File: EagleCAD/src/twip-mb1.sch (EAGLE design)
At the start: 13 parts, among them U1 GY-521MPU6050

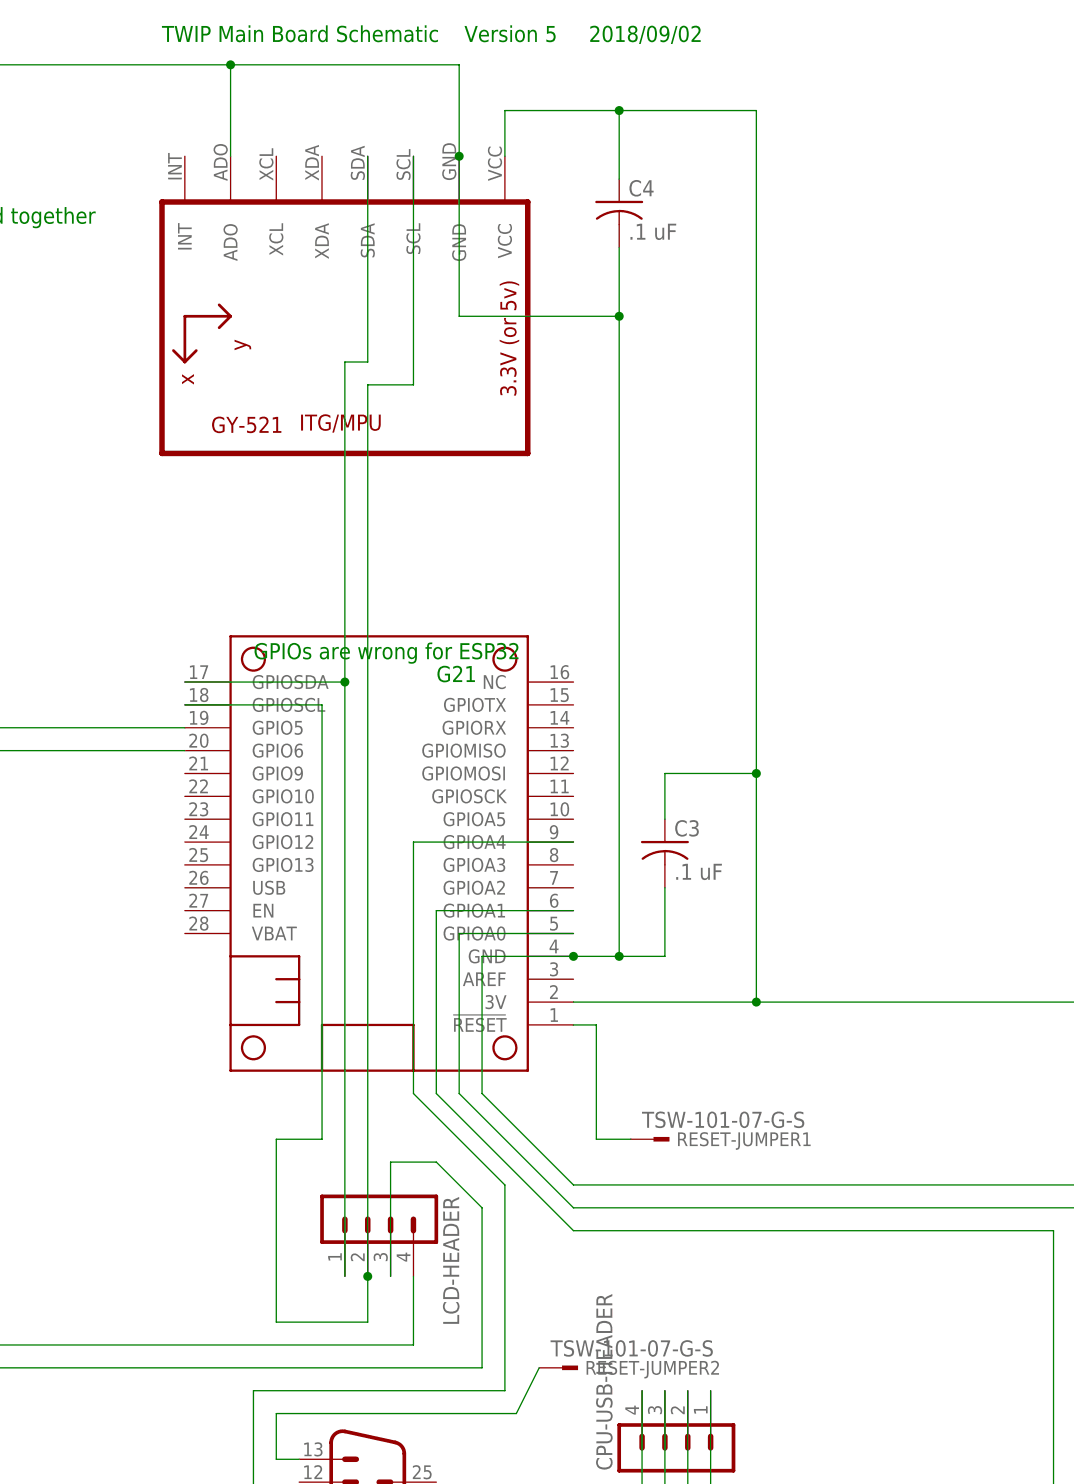
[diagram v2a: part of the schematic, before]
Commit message: separate I2C buses with pullups
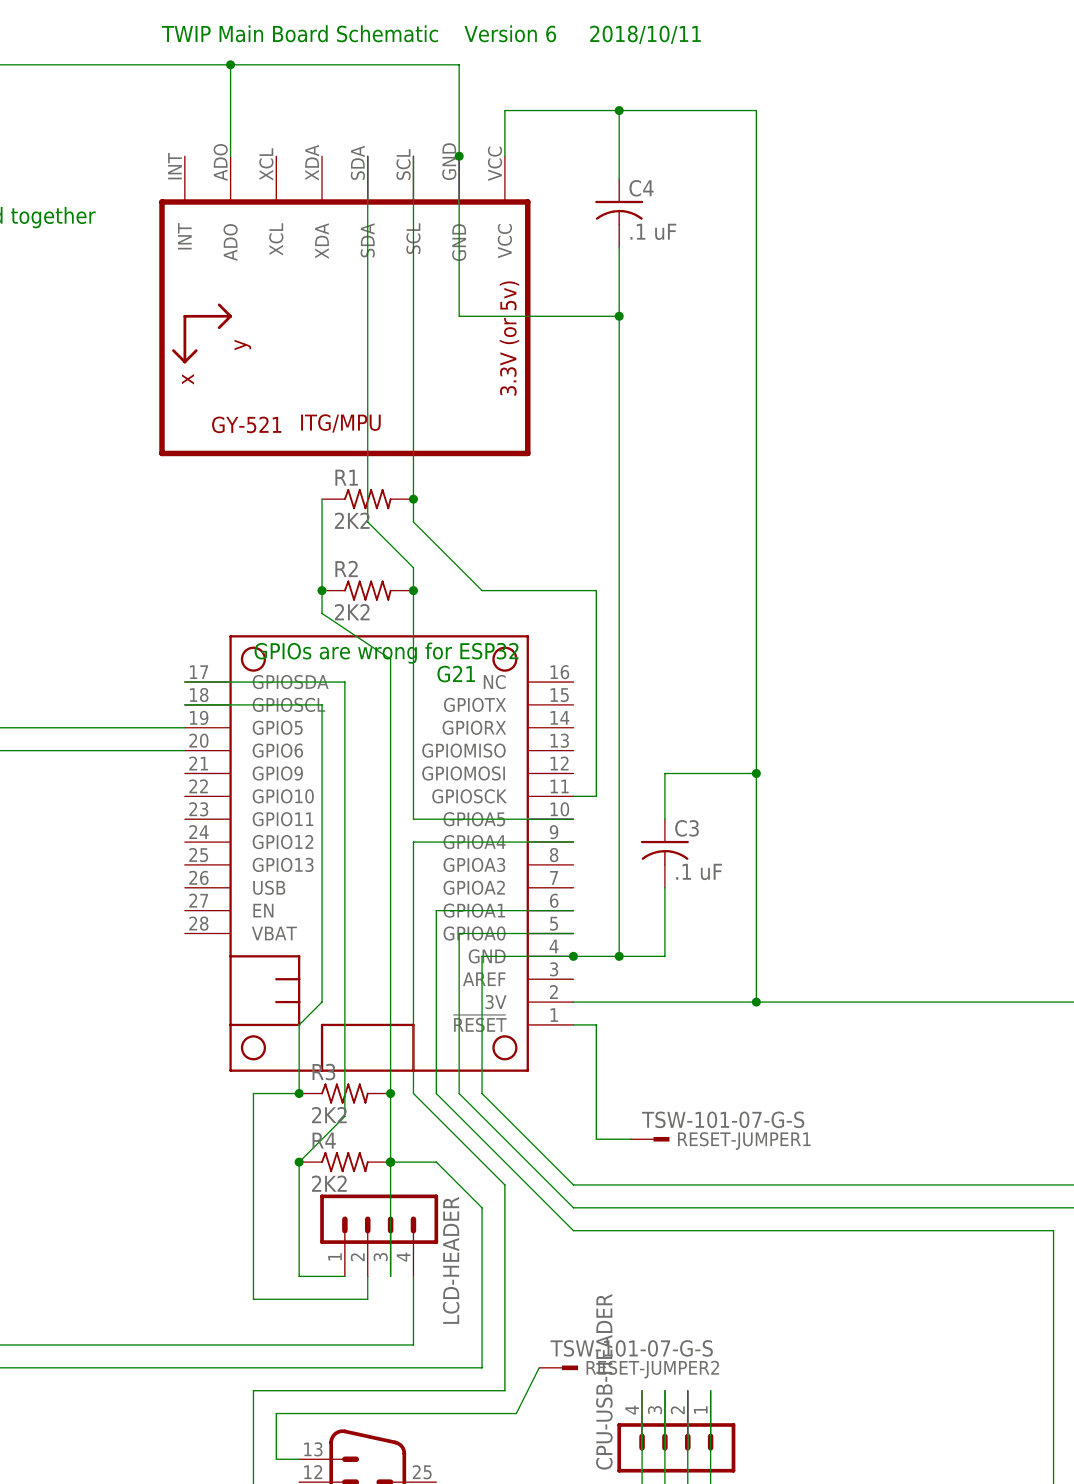
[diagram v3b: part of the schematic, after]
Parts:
- added R1, R2, R3, R4: 2K2, resistor:R-US_0309/12
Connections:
- new net N$17: MS2.GPIOSCK, R1.2, U1.SCL
- new net N$25: MS2.GPIOA5, R2.2, U1.SDA
- net 3V: now also R1.1, R2.1, R3.2, R4.2
- net N$11: now also R3.1; no longer U1.SCL
- net N$19: now also R4.1; no longer U1.SDA
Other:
- note added: "TWIP Main Board Schematic Version 6 2018/10/11"
- note removed: "TWIP Main Board Schematic Version 5 2018/09/02"
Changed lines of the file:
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@@
 <part name="C3" library="rcl" library_urn="urn:adsk.eagle:library:334" deviceset="C-US" device="025-024X044" package3d_urn="urn:adsk.eagle:package:23630/1" value=".1 uF"/>
 <part name="C4" library="rcl" library_urn="urn:adsk.eagle:library:334" deviceset="C-US" device="025-024X044" package3d_urn="urn:adsk.eagle:package:23630/1" value=".1 uF"/>
+<part name="R1" library="resistor" library_urn="urn:adsk.eagle:library:348" deviceset="R-US_" device="0309/12" package3d_urn="urn:adsk.eagle:package:26089/1" value="    2K2"/>
+<part name="R2" library="resistor" library_urn="urn:adsk.eagle:library:348" deviceset="R-US_" device="0309/12" package3d_urn="urn:adsk.eagle:package:26089/1" value="    2K2"/>
+<part name="R3" library="resistor" library_urn="urn:adsk.eagle:library:348" deviceset="R-US_" device="0309/12" package3d_urn="urn:adsk.eagle:package:26089/1" value="    2K2"/>
+<part name="R4" library="resistor" library_urn="urn:adsk.eagle:library:348" deviceset="R-US_" device="0309/12" package3d_urn="urn:adsk.eagle:package:26089/1" value="    2K2"/>
 </parts>
 <sheets>
@@
 <text x="43.18" y="198.12" size="1.778" layer="91">Need to connect 12V ground and 5V ground together
 as a place that isolates motor noise</text>
-<text x="109.22" y="220.98" size="1.778" layer="91">TWIP Main Board Schematic    Version 5     2018/09/02</text>
+<text x="109.22" y="220.98" size="1.778" layer="91">TWIP Main Board Schematic    Version 6     2018/10/11</text>
 </plain>
 <instances>
@@
 <instance part="C3" gate="G$1" x="165.1" y="132.08"/>
 <instance part="C4" gate="G$1" x="160.02" y="203.2"/>
+<instance part="R1" gate="G$1" x="132.08" y="170.18"/>
+<instance part="R2" gate="G$1" x="132.08" y="160.02"/>
+<instance part="R3" gate="G$1" x="129.54" y="104.14"/>
+<instance part="R4" gate="G$1" x="129.54" y="96.52"/>
 </instances>
 <busses>
@@
 <net name="N$19" class="0">
 <segment>
-<wire x1="129.54" y1="149.86" x2="129.54" y2="185.42" width="0.1524" layer="91"/>
-<wire x1="129.54" y1="185.42" x2="132.08" y2="185.42" width="0.1524" layer="91"/>
-<pinref part="U1" gate="G$1" pin="SDA"/>
-<wire x1="132.08" y1="185.42" x2="132.08" y2="208.28" width="0.1524" layer="91"/>
 <pinref part="MS2" gate="G$1" pin="GPIOSDA"/>
 <wire x1="111.76" y1="149.86" x2="129.54" y2="149.86" width="0.1524" layer="91"/>
 <pinref part="LCD-HEADER" gate="1" pin="1"/>
-<wire x1="129.54" y1="149.86" x2="129.54" y2="83.82" width="0.1524" layer="91"/>
-<junction x="129.54" y="149.86"/>
+<wire x1="129.54" y1="149.86" x2="129.54" y2="101.6" width="0.1524" layer="91"/>
+<pinref part="R4" gate="G$1" pin="1"/>
+<junction x="124.46" y="96.52"/>
+<wire x1="124.46" y1="96.52" x2="129.54" y2="101.6" width="0.1524" layer="91"/>
+<wire x1="129.54" y1="83.82" x2="124.46" y2="83.82" width="0.1524" layer="91"/>
+<wire x1="124.46" y1="83.82" x2="124.46" y2="96.52" width="0.1524" layer="91"/>
 </segment>
 </net>
@@
 <wire x1="165.1" y1="139.7" x2="175.26" y2="139.7" width="0.1524" layer="91"/>
 <junction x="175.26" y="139.7"/>
+<junction x="134.62" y="96.52"/>
+<wire x1="134.62" y1="96.52" x2="134.62" y2="104.14" width="0.1524" layer="91"/>
+<wire x1="134.62" y1="104.14" x2="134.62" y2="152.4" width="0.1524" layer="91"/>
+<wire x1="134.62" y1="152.4" x2="127" y2="157.48" width="0.1524" layer="91"/>
+<wire x1="127" y1="157.48" x2="127" y2="160.02" width="0.1524" layer="91"/>
+<pinref part="R1" gate="G$1" pin="1"/>
+<pinref part="R2" gate="G$1" pin="1"/>
+<wire x1="127" y1="160.02" x2="127" y2="170.18" width="0.1524" layer="91"/>
+<junction x="127" y="160.02"/>
+<pinref part="R3" gate="G$1" pin="2"/>
+<junction x="134.62" y="104.14"/>
+<pinref part="R4" gate="G$1" pin="2"/>
+<junction x="134.62" y="96.52"/>
 </segment>
 </net>
@@
 <net name="N$11" class="0">
 <segment>
-<pinref part="U1" gate="G$1" pin="SCL"/>
-<wire x1="137.16" y1="182.88" x2="137.16" y2="208.28" width="0.1524" layer="91"/>
-<wire x1="137.16" y1="182.88" x2="132.08" y2="182.88" width="0.1524" layer="91"/>
 <pinref part="LCD-HEADER" gate="1" pin="2"/>
-<wire x1="132.08" y1="182.88" x2="132.08" y2="83.82" width="0.1524" layer="91"/>
-<wire x1="132.08" y1="83.82" x2="132.08" y2="78.74" width="0.1524" layer="91"/>
-<junction x="132.08" y="83.82"/>
-<wire x1="121.92" y1="99.06" x2="121.92" y2="78.74" width="0.1524" layer="91"/>
-<wire x1="127" y1="99.06" x2="121.92" y2="99.06" width="0.1524" layer="91"/>
-<wire x1="127" y1="147.32" x2="127" y2="99.06" width="0.1524" layer="91"/>
+<wire x1="132.08" y1="83.82" x2="132.08" y2="81.28" width="0.1524" layer="91"/>
+<wire x1="127" y1="147.32" x2="127" y2="114.3" width="0.1524" layer="91"/>
 <pinref part="MS2" gate="G$1" pin="GPIOSCL"/>
 <wire x1="111.76" y1="147.32" x2="127" y2="147.32" width="0.1524" layer="91"/>
-<wire x1="132.08" y1="78.74" x2="121.92" y2="78.74" width="0.1524" layer="91"/>
+<wire x1="132.08" y1="81.28" x2="119.38" y2="81.28" width="0.1524" layer="91"/>
+<wire x1="127" y1="114.3" x2="124.46" y2="111.76" width="0.1524" layer="91"/>
+<pinref part="R3" gate="G$1" pin="1"/>
+<wire x1="124.46" y1="111.76" x2="124.46" y2="104.14" width="0.1524" layer="91"/>
+<junction x="124.46" y="104.14"/>
+<wire x1="124.46" y1="104.14" x2="119.38" y2="104.14" width="0.1524" layer="91"/>
+<wire x1="119.38" y1="104.14" x2="119.38" y2="81.28" width="0.1524" layer="91"/>
 </segment>
 </net>
@@
 </segment>
 </net>
+<net name="N$17" class="0">
+<segment>
+<pinref part="U1" gate="G$1" pin="SCL"/>
+<wire x1="137.16" y1="208.28" x2="137.16" y2="170.18" width="0.1524" layer="91"/>
+<wire x1="137.16" y1="170.18" x2="137.16" y2="167.64" width="0.1524" layer="91"/>
+<wire x1="144.78" y1="160.02" x2="157.48" y2="160.02" width="0.1524" layer="91"/>
+<wire x1="157.48" y1="160.02" x2="157.48" y2="137.16" width="0.1524" layer="91"/>
+<pinref part="MS2" gate="G$1" pin="GPIOSCK"/>
+<wire x1="157.48" y1="137.16" x2="154.94" y2="137.16" width="0.1524" layer="91"/>
+<wire x1="137.16" y1="167.64" x2="144.78" y2="160.02" width="0.1524" layer="91"/>
+<pinref part="R1" gate="G$1" pin="2"/>
+<junction x="137.16" y="170.18"/>
+</segment>
+</net>
+<net name="N$25" class="0">
+<segment>
+<pinref part="U1" gate="G$1" pin="SDA"/>
+<wire x1="132.08" y1="208.28" x2="132.08" y2="167.64" width="0.1524" layer="91"/>
+<pinref part="MS2" gate="G$1" pin="GPIOA5"/>
+<wire x1="137.16" y1="134.62" x2="154.94" y2="134.62" width="0.1524" layer="91"/>
+<wire x1="137.16" y1="134.62" x2="137.16" y2="160.02" width="0.1524" layer="91"/>
+<wire x1="137.16" y1="160.02" x2="137.16" y2="162.56" width="0.1524" layer="91"/>
+<wire x1="137.16" y1="162.56" x2="132.08" y2="167.64" width="0.1524" layer="91"/>
+<pinref part="R2" gate="G$1" pin="2"/>
+<junction x="137.16" y="160.02"/>
+</segment>
+</net>

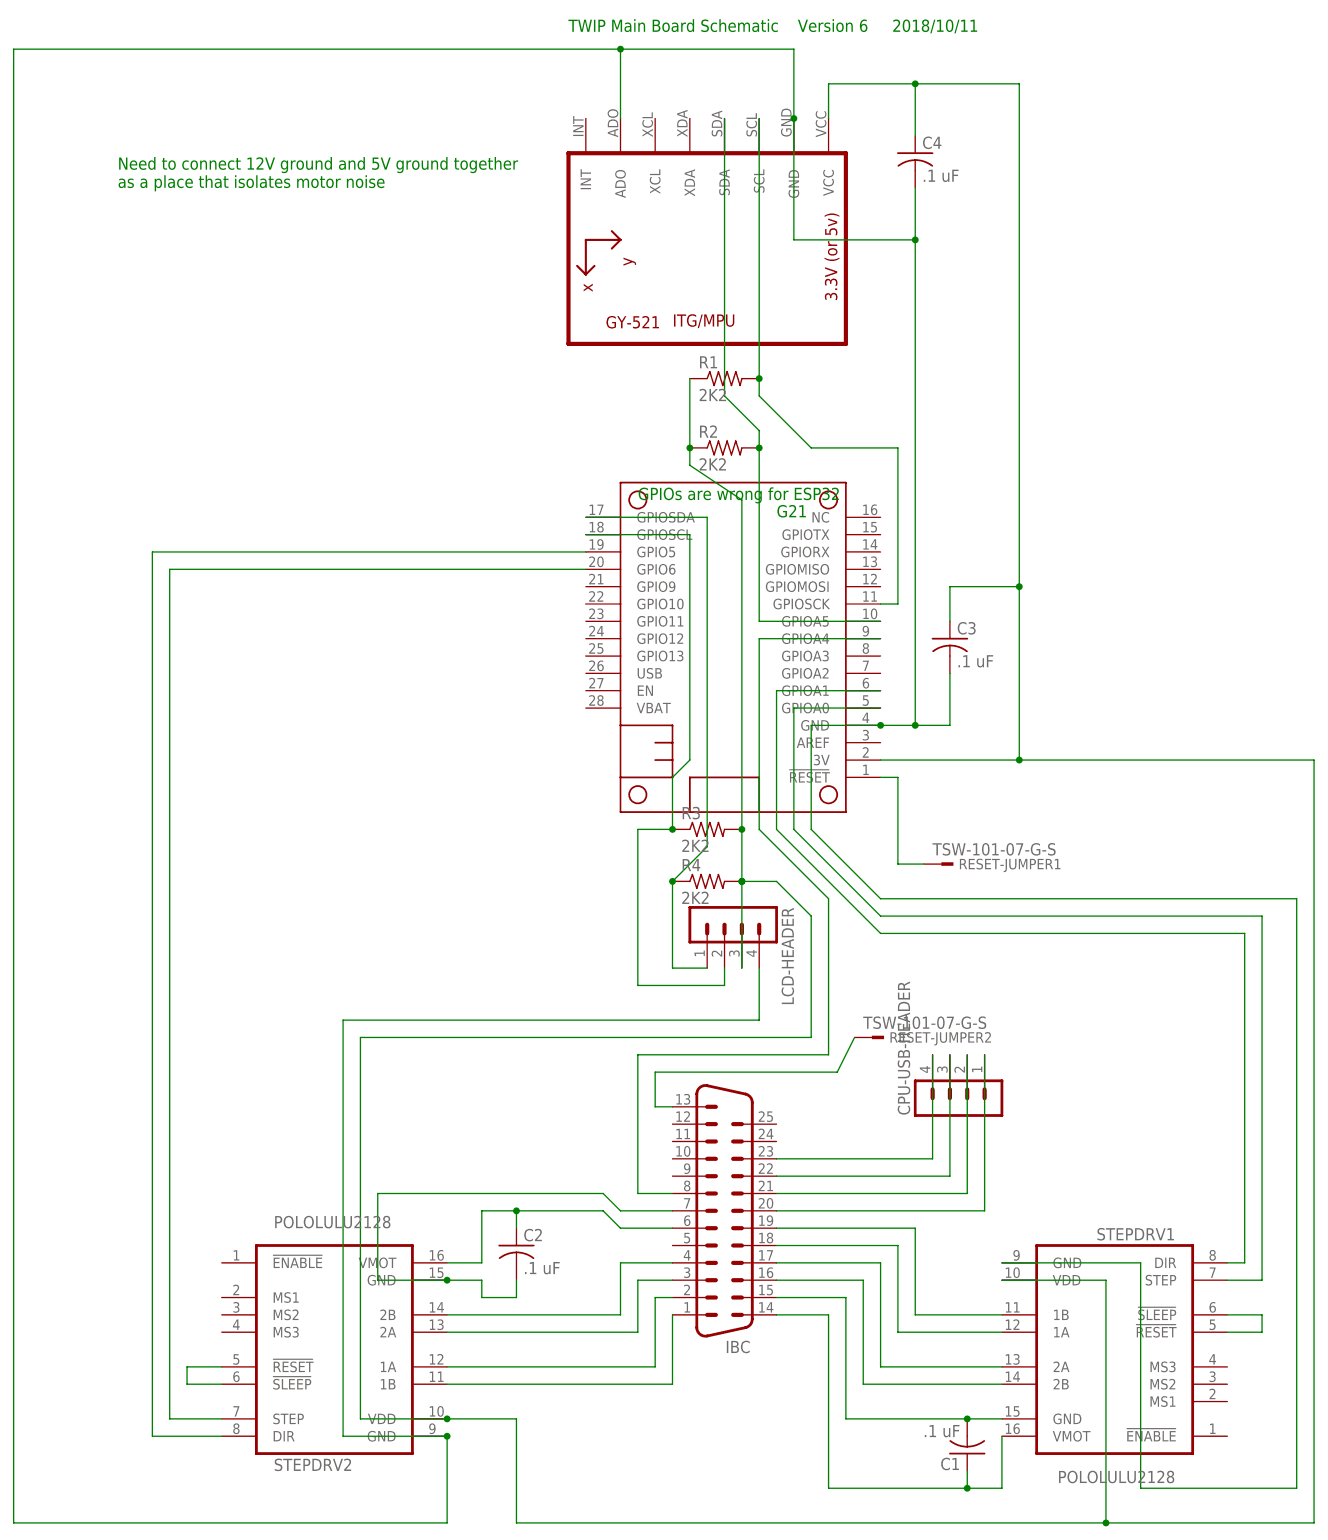
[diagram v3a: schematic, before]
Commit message: widen all traces from .006 to .012 inch
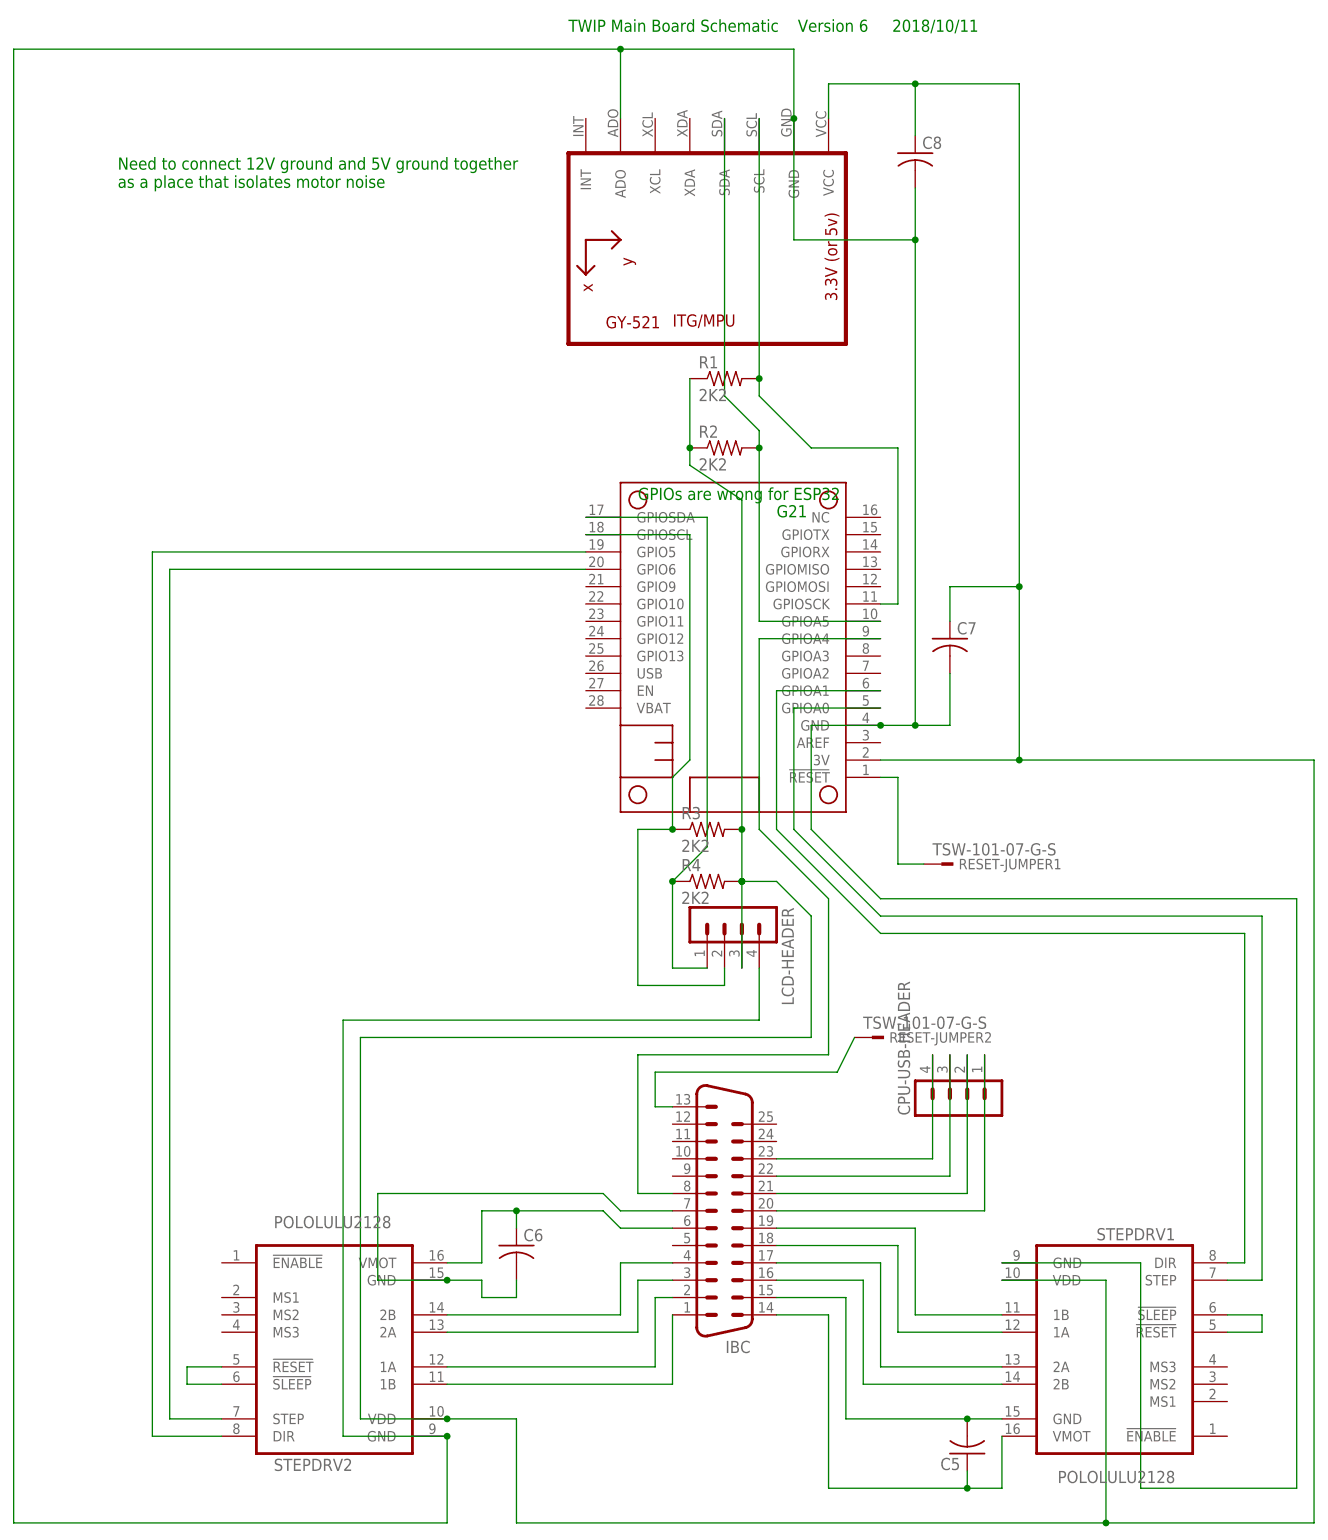
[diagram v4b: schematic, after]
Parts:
- removed C1, C2, C3, C4: .1 uF, rcl:C-US025-024X044
- added C5, C6, C7, C8: (no value), rcl:C-US050-024X044
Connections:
- net 3V: now also C7.1, C8.1; no longer C3.1, C4.1
- net N$2: now also C6.2; no longer C2.2
- net N$20: now also C5.2; no longer C1.2
- net N$21: now also C6.1; no longer C2.1
- net N$22: now also C5.1; no longer C1.1
- net N$35: now also C7.2, C8.2; no longer C3.2, C4.2
